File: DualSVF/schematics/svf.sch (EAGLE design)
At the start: 34 parts, among them IC1 SSM2164S, IC2 TL074

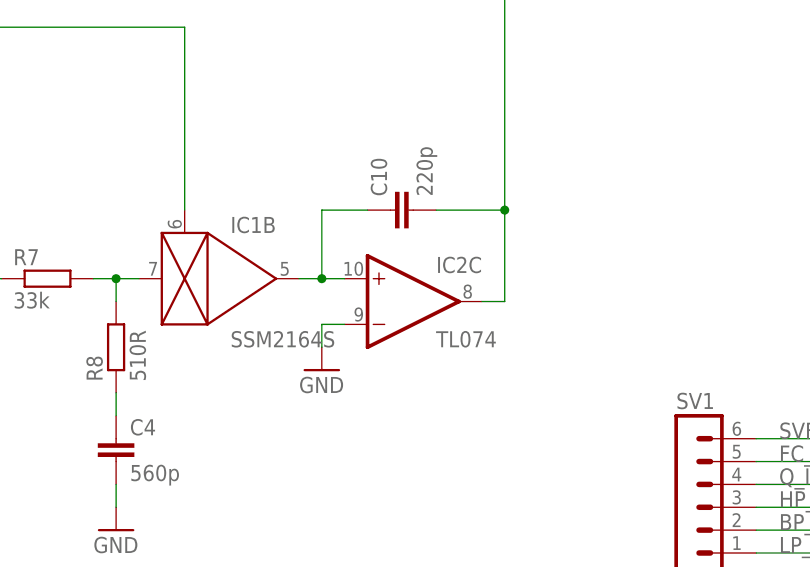
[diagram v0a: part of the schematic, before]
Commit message: Changes to SVF .brd and .sch
Alterations to correct final integrator stage
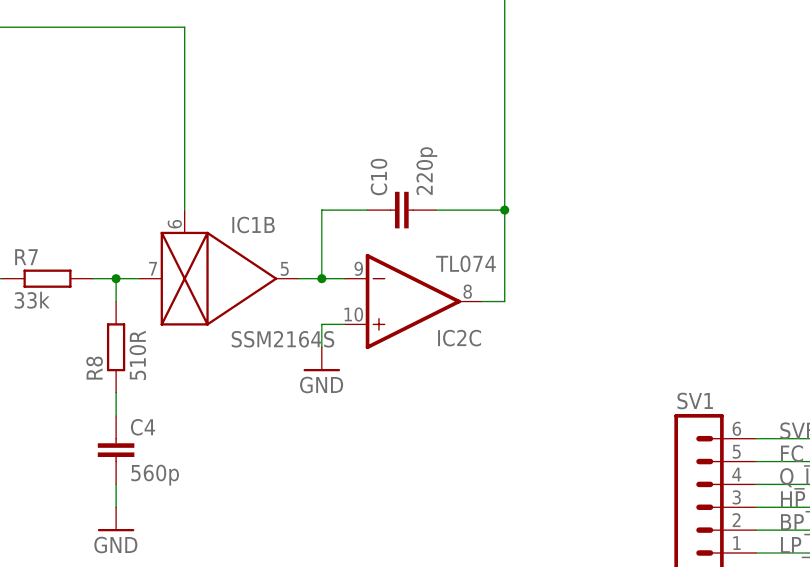
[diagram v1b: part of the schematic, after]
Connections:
- removed net N$5: C10.1, IC1B.OUT, IC2C.+IN
- new net N$3: C10.1, IC1B.OUT, IC2C.-IN
- net GND: now also IC2C.+IN; no longer IC2C.-IN
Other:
- moved on the sheet: IC2C
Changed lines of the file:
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@@
 <?xml version="1.0" encoding="utf-8"?>
 <!DOCTYPE eagle SYSTEM "eagle.dtd">
-<eagle version="7.5.0">
+<eagle version="7.7.0">
 <drawing>
 <settings>
@@
 <instance part="IC1" gate="D" x="-30.48" y="-101.6"/>
 <instance part="R12" gate="G$1" x="-55.88" y="-7.62"/>
-<instance part="IC2" gate="C" x="83.82" y="-7.62"/>
+<instance part="IC2" gate="C" x="83.82" y="-7.62" rot="MR180"/>
 <instance part="IC2" gate="D" x="-25.4" y="-53.34" rot="R180"/>
 <instance part="TP1" gate="G$1" x="15.24" y="27.94"/>
@@
 </segment>
 <segment>
-<pinref part="GND2" gate="1" pin="GND"/>
-<wire x1="76.2" y1="-10.16" x2="73.66" y2="-10.16" width="0.1524" layer="91"/>
-<wire x1="73.66" y1="-10.16" x2="73.66" y2="-12.7" width="0.1524" layer="91"/>
-<pinref part="IC2" gate="C" pin="-IN"/>
-</segment>
-<segment>
 <pinref part="GND10" gate="1" pin="GND"/>
 <pinref part="IC1" gate="E" pin="GND"/>
@@
 <wire x1="121.92" y1="-99.06" x2="129.54" y2="-99.06" width="0.1524" layer="91"/>
 <wire x1="129.54" y1="-99.06" x2="129.54" y2="-109.22" width="0.1524" layer="91"/>
+</segment>
+<segment>
+<pinref part="GND2" gate="1" pin="GND"/>
+<wire x1="73.66" y1="-12.7" x2="73.66" y2="-10.16" width="0.1524" layer="91"/>
+<pinref part="IC2" gate="C" pin="+IN"/>
+<wire x1="73.66" y1="-10.16" x2="76.2" y2="-10.16" width="0.1524" layer="91"/>
 </segment>
 </net>
@@
 <net name="LP_OUT" class="0">
 <segment>
-<wire x1="91.44" y1="-7.62" x2="93.98" y2="-7.62" width="0.1524" layer="91"/>
 <pinref part="C10" gate="G$1" pin="2"/>
 <wire x1="86.36" y1="2.54" x2="93.98" y2="2.54" width="0.1524" layer="91"/>
@@
 <wire x1="93.98" y1="38.1" x2="-63.5" y2="38.1" width="0.1524" layer="91"/>
 <label x="-78.74" y="38.1" size="1.778" layer="95"/>
-<pinref part="IC2" gate="C" pin="OUT"/>
 <pinref part="R15" gate="G$1" pin="1"/>
 <wire x1="-63.5" y1="38.1" x2="-78.74" y2="38.1" width="0.1524" layer="91"/>
@@
 <wire x1="-63.5" y1="15.24" x2="-63.5" y2="38.1" width="0.1524" layer="91"/>
 <junction x="-63.5" y="38.1"/>
+<pinref part="IC2" gate="C" pin="OUT"/>
+<wire x1="91.44" y1="-7.62" x2="93.98" y2="-7.62" width="0.1524" layer="91"/>
 </segment>
 <segment>
@@
 <wire x1="121.92" y1="-35.56" x2="139.7" y2="-35.56" width="0.1524" layer="91"/>
 <label x="124.46" y="-35.56" size="1.778" layer="95"/>
-</segment>
-</net>
-<net name="N$5" class="0">
-<segment>
-<wire x1="71.12" y1="-5.08" x2="73.66" y2="-5.08" width="0.1524" layer="91"/>
-<pinref part="C10" gate="G$1" pin="1"/>
-<wire x1="73.66" y1="-5.08" x2="76.2" y2="-5.08" width="0.1524" layer="91"/>
-<wire x1="78.74" y1="2.54" x2="73.66" y2="2.54" width="0.1524" layer="91"/>
-<wire x1="73.66" y1="2.54" x2="73.66" y2="-5.08" width="0.1524" layer="91"/>
-<junction x="73.66" y="-5.08"/>
-<pinref part="IC1" gate="B" pin="OUT"/>
-<pinref part="IC2" gate="C" pin="+IN"/>
 </segment>
 </net>
@@
 </segment>
 </net>
+<net name="N$3" class="0">
+<segment>
+<pinref part="IC2" gate="C" pin="-IN"/>
+<pinref part="IC1" gate="B" pin="OUT"/>
+<wire x1="76.2" y1="-5.08" x2="73.66" y2="-5.08" width="0.1524" layer="91"/>
+<pinref part="C10" gate="G$1" pin="1"/>
+<wire x1="73.66" y1="-5.08" x2="71.12" y2="-5.08" width="0.1524" layer="91"/>
+<wire x1="78.74" y1="2.54" x2="73.66" y2="2.54" width="0.1524" layer="91"/>
+<wire x1="73.66" y1="-5.08" x2="73.66" y2="2.54" width="0.1524" layer="91"/>
+<junction x="73.66" y="-5.08"/>
+</segment>
+</net>
